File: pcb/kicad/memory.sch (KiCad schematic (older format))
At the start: 5 parts, among them U12 MT45W8MW16, U13 CY62148EV30-BVXI

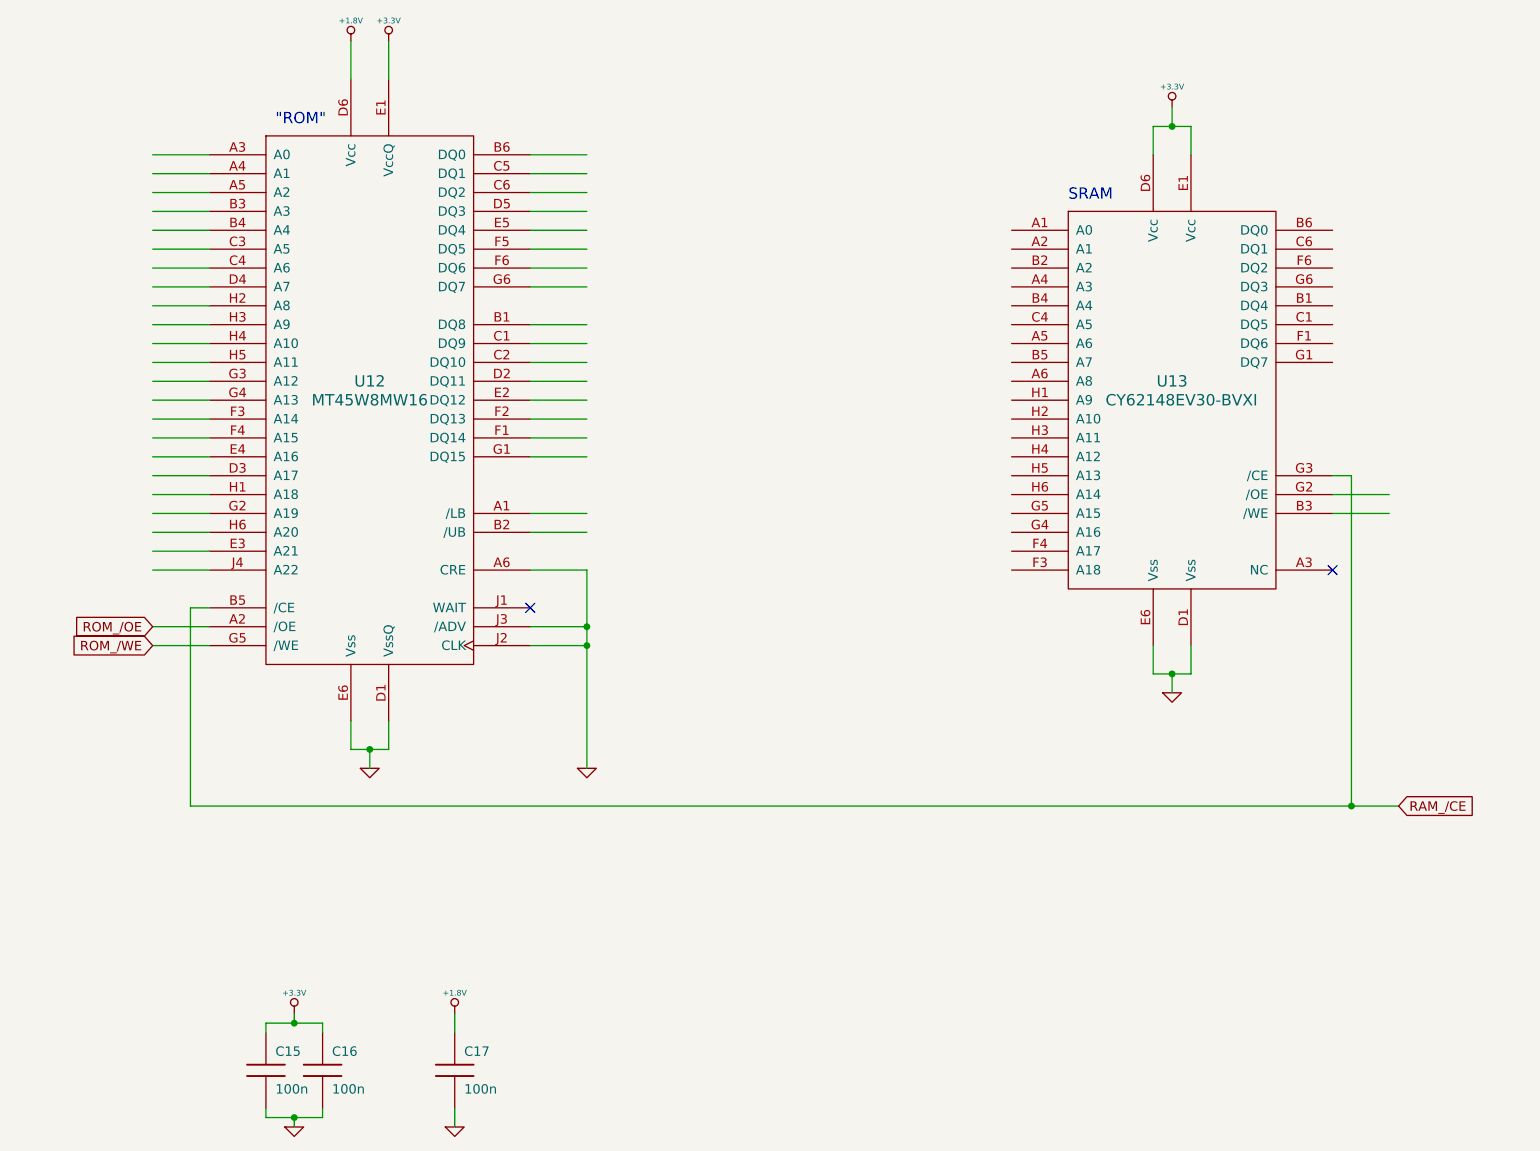
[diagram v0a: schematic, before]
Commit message: Schematics: connect PSRAM
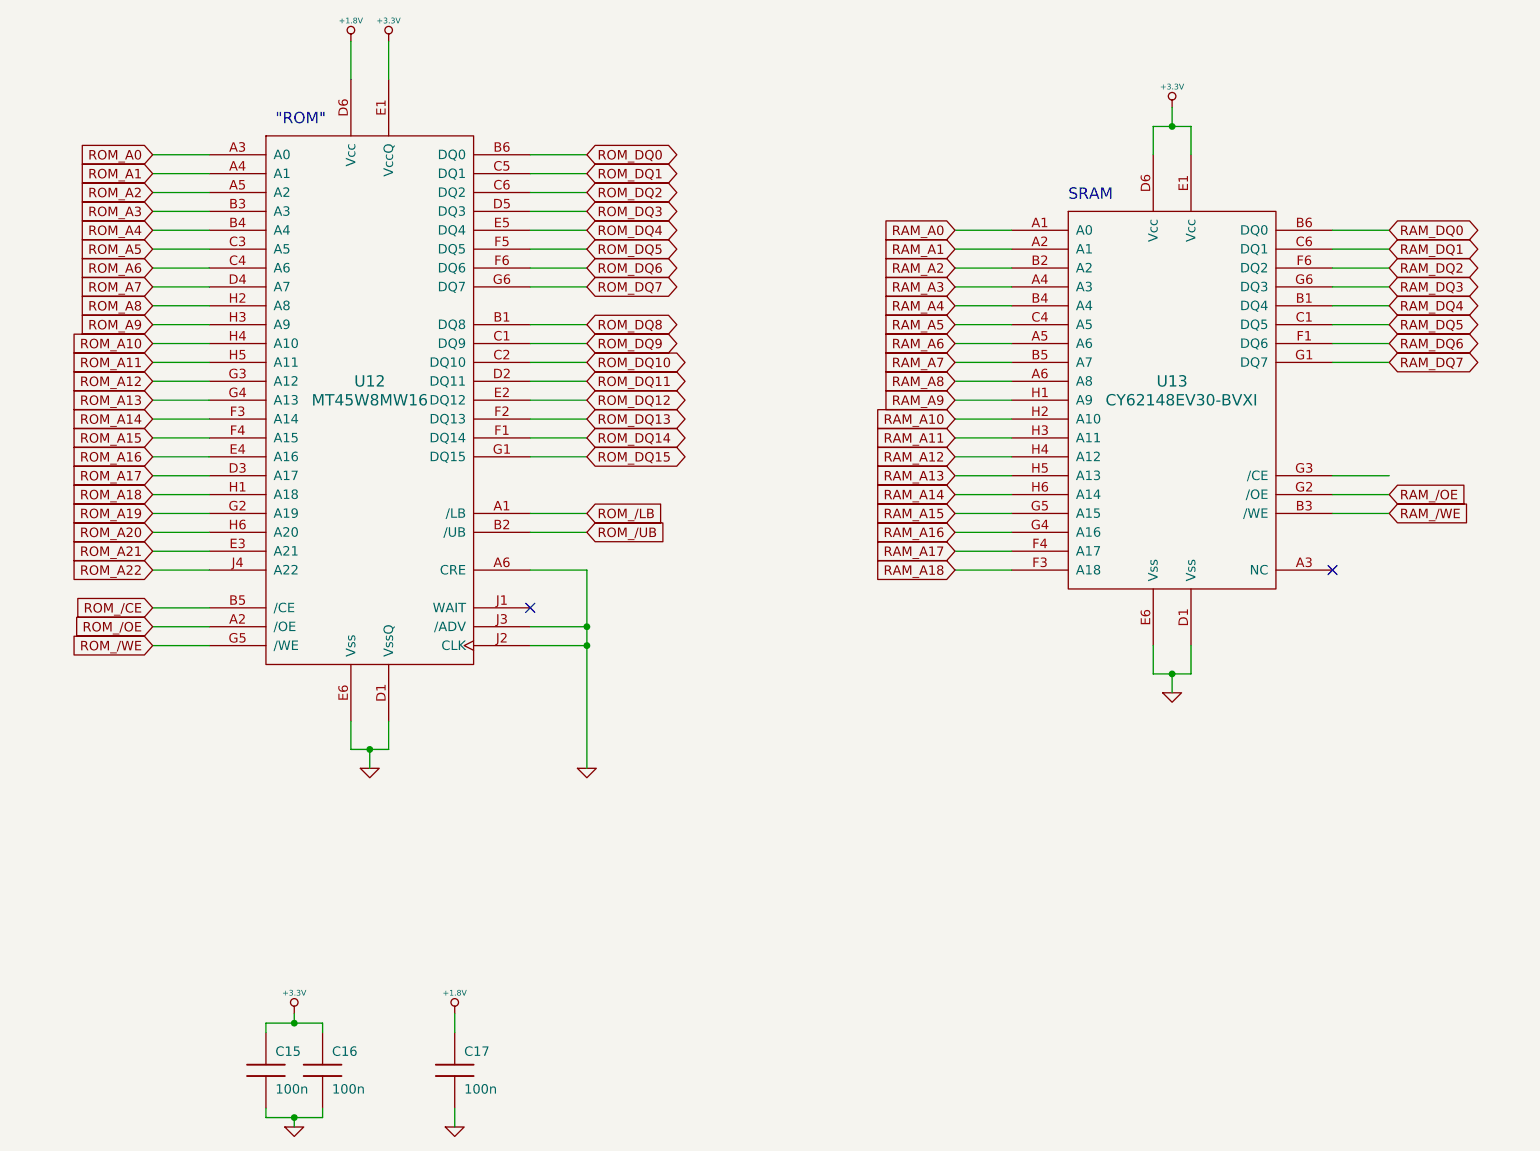
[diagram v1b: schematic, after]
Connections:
- net labels added: RAM_/OE, RAM_/WE, RAM_A0, RAM_A1, RAM_A10, RAM_A11, RAM_A12, RAM_A13, RAM_A14, RAM_A15, RAM_A16, RAM_A17, RAM_A18, RAM_A2, RAM_A3, RAM_A4, RAM_A5, RAM_A6, RAM_A7, RAM_A8, RAM_A9, RAM_DQ0, RAM_DQ1, RAM_DQ2, RAM_DQ3, RAM_DQ4, RAM_DQ5, RAM_DQ6, RAM_DQ7, ROM_/CE, ROM_/LB, ROM_/UB, ROM_A0, ROM_A1, ROM_A10, ROM_A11, ROM_A12, ROM_A13, ROM_A14, ROM_A15, ROM_A16, ROM_A17, ROM_A18, ROM_A19, ROM_A2, ROM_A20, ROM_A21, ROM_A22, ROM_A3, ROM_A4, ROM_A5, ROM_A6, ROM_A7, ROM_A8, ROM_A9, ROM_DQ0, ROM_DQ1, ROM_DQ10, ROM_DQ11, ROM_DQ12, ROM_DQ13, ROM_DQ14, ROM_DQ15, ROM_DQ2, ROM_DQ3, ROM_DQ4, ROM_DQ5, ROM_DQ6, ROM_DQ7, ROM_DQ8, ROM_DQ9
- net labels removed: RAM_/CE
- wire segments 78 -> 109

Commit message: pcb wip
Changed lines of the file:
@@
-EESchema Schematic File Version 2  date Thu 22 Apr 2010 07:50:14 PM CEST
+EESchema Schematic File Version 2  date Sat 15 May 2010 02:07:58 AM CEST
 LIBS:power
 LIBS:device
@@
 Sheet 3 6
 Title "sd2snes Mark II"
-Date "22 apr 2010"
+Date "14 may 2010"
 Rev "A"
 Comp "Maximilian Rehkopf"
@@
 Connection ~ 4550 4650
 Wire Wire Line
-	4550 5400 4550 4750
-Wire Wire Line
-	4550 4750 4550 4650
-Wire Wire Line
-	4550 4650 4550 4350
+	4550 5400 4550 4350
 Connection ~ 4550 4750
 Wire Wire Line
@@
 	3000 6700 3000 6750
 Wire Wire Line
-	2850 6750 2850 6800
+	2850 6800 2850 6750
 Connection ~ 3000 7250
 Wire Wire Line
-	2850 7250 3000 7250
-Wire Wire Line
-	3000 7250 3150 7250
+	2850 7250 3150 7250
 Wire Wire Line
 	2850 7250 2850 7200
@@
 Connection ~ 7650 4900
 Wire Wire Line
-	7750 4900 7650 4900
-Wire Wire Line
-	7650 4900 7550 4900
+	7750 4900 7550 4900
 Wire Wire Line
 	7750 4900 7750 4750
 Connection ~ 3400 5300
 Wire Wire Line
-	3500 5300 3400 5300
-Wire Wire Line
-	3400 5300 3300 5300
+	3500 5300 3300 5300
 Wire Wire Line
 	3500 5300 3500 5150
@@
 Connection ~ 7650 2000
 Wire Wire Line
-	7750 2000 7650 2000
-Wire Wire Line
-	7650 2000 7550 2000
+	7750 2000 7550 2000
 Wire Wire Line
 	7750 2000 7750 2150
@@
 	3850 6800 3850 6700
 Wire Wire Line
-	3150 6750 3150 6800
+	3150 6800 3150 6750
 Wire Wire Line
-	2850 6750 3000 6750
-Wire Wire Line
-	3000 6750 3150 6750
+	3150 6750 2850 6750
 Connection ~ 3000 6750
 Wire Wire Line

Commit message: pcb wip
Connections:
- net RAM_/CE: now reaches U13.G3 (/CE)

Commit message: pcb wip
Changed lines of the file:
@@
-EESchema Schematic File Version 2  date Sat 15 May 2010 04:06:22 PM CEST
+EESchema Schematic File Version 2  date Sun 16 May 2010 01:08:34 AM CEST
 LIBS:power
 LIBS:device
@@
 	3000 6700 3000 6750
 Wire Wire Line
-	2850 6750 2850 6800
+	2850 6800 2850 6750
 Connection ~ 3000 7250
 Wire Wire Line
@@
 	3850 6800 3850 6700
 Wire Wire Line
-	3150 6750 3150 6800
-Wire Wire Line
-	2850 6750 3150 6750
+	3150 6800 3150 6750
+Wire Wire Line
+	3150 6750 2850 6750
 Connection ~ 3000 6750
 Wire Wire Line

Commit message: pcb wip
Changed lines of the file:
@@
-EESchema Schematic File Version 2  date Sun 16 May 2010 01:45:32 AM CEST
+EESchema Schematic File Version 2  date Sun 16 May 2010 04:32:38 PM CEST
 LIBS:power
 LIBS:device
@@
 LIBS:cs4344
 LIBS:double_sch_kcom
+LIBS:usb_minib
 LIBS:sd2snes-cache
 EELAYER 24  0
@@
 Sheet 3 6
 Title "sd2snes Mark II"
-Date "15 may 2010"
+Date "16 may 2010"
 Rev "A"
 Comp "Maximilian Rehkopf"
@@
 Text Label 4350 4650 0    50   ~ 0
 ROM_/ADV
-Text Label 4350 4350 0    50   ~ 0
-ROM_CRE
 Text Label 4350 4150 0    50   ~ 0
 ROM_/UB
